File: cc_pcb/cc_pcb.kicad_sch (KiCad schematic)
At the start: 58 parts, among them J1 Conn_02x05_Odd_Even, J2 Controller (40Pin->SPI), J3 Wi-Fi Module, J4 RFID Scanner, J5 SD Card Reader, J6 4x4 Keypad, SW1 SW_Push, U1 LD1117S33TR_SOT223, U2 STM32F091RCTx, U3 LM393

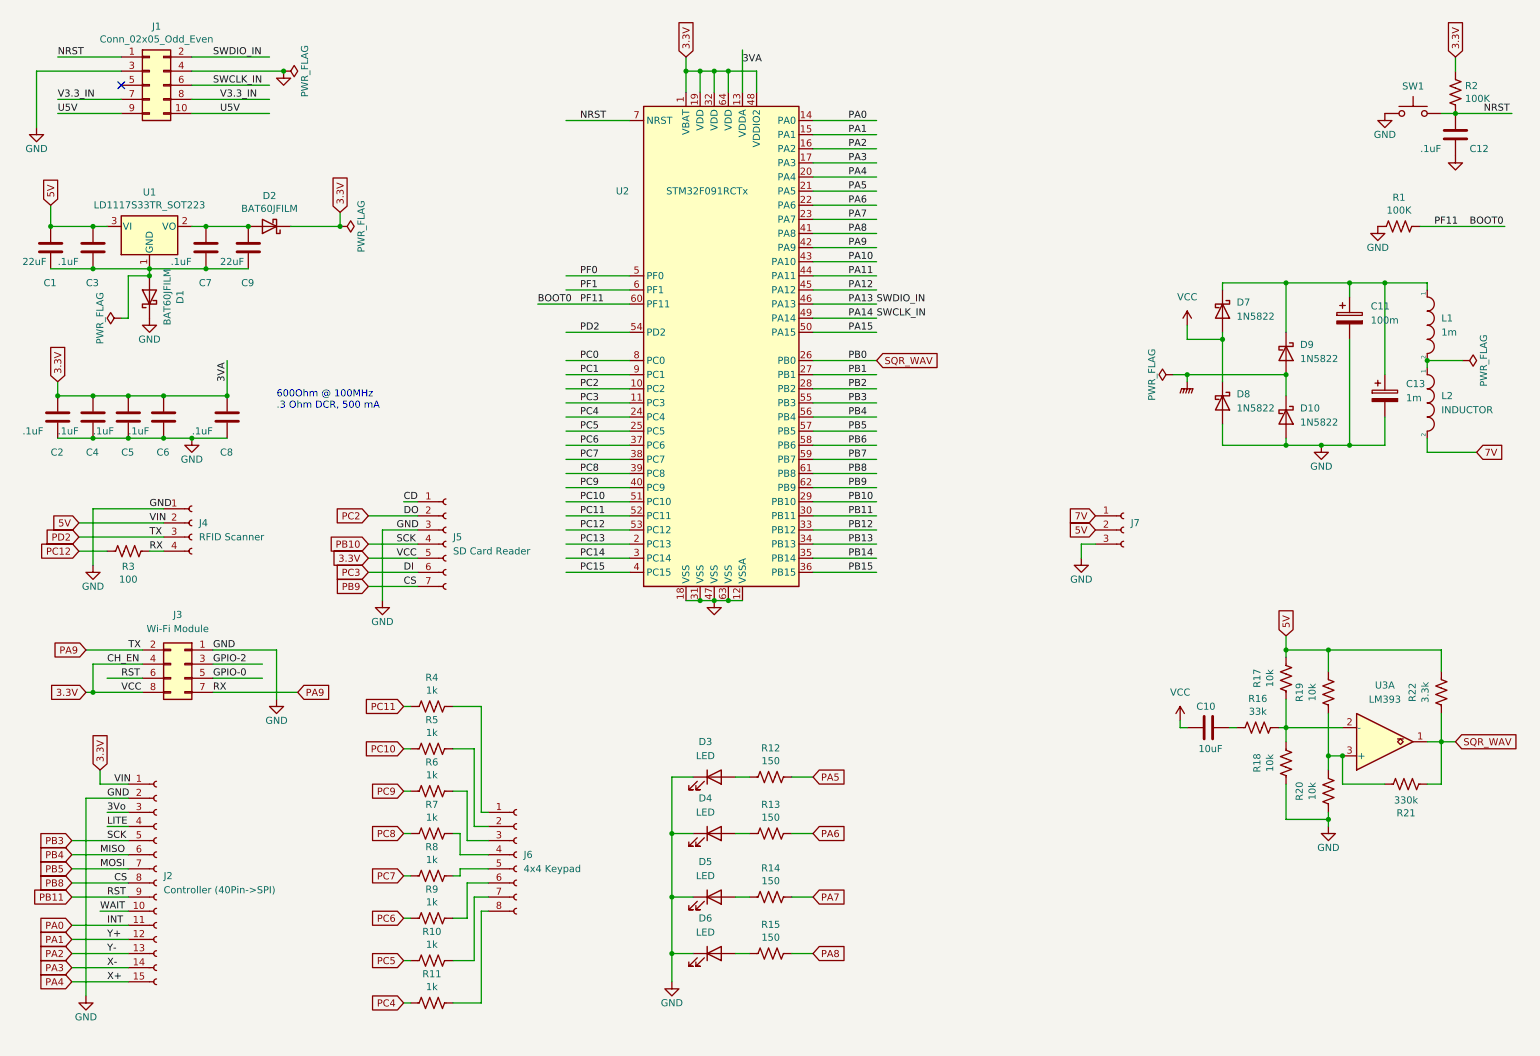
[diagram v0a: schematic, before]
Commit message: organized schematic and separated power supply by modules and our design
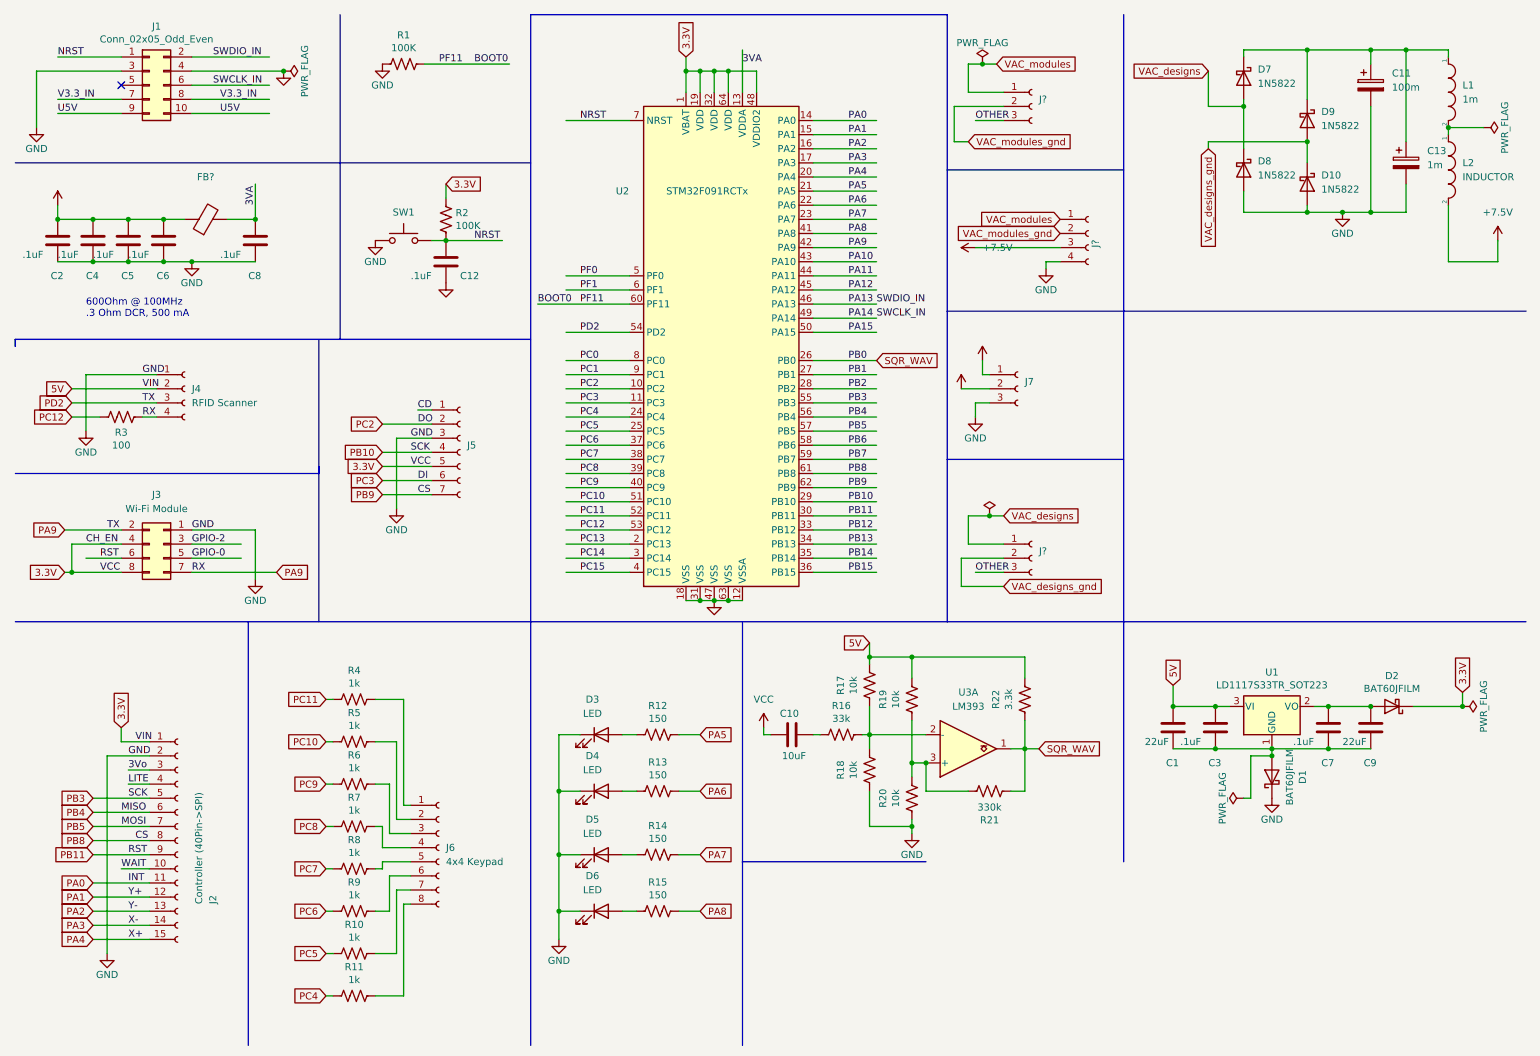
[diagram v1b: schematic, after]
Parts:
- added FB?: (no value), symbol Device:FerriteBead
- added J? (x2): (no value), symbol Connector:Conn_01x03_Female
- added J?: (no value), symbol Connector:Conn_01x04_Female
- J5: value SD Card Reader -> (none)
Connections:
- net GND: now also J?.4 (Pin_4)
- net VCC: no longer C2.1, C4.1, C5.1, C6.1, C8.1, D7.2 (A), D8.1 (K), J7.2 (Pin_2), U2.13 (VDDA)
- net 7V renamed +7.5V
- net +7.5V: now also J?.3 (Pin_3)
- net GNDPWR renamed VAC_designs_gnd
- net VAC_designs_gnd: now also J?.2 (Pin_2)
- new net +3V3: C2.1, C4.1, C5.1, C6.1, FB?.1
- new net +5V: J7.2 (Pin_2)
- new net 3VA: C8.1, FB?.2, U2.13 (VDDA)
- new net OTHER: J?.3 (Pin_3), J?.3 (Pin_3)
- new net VAC_designs: D7.2 (A), D8.1 (K), J?.1 (Pin_1)
- new net VAC_modules: J?.1 (Pin_1), J?.1 (Pin_1)
- new net VAC_modules_gnd: J?.2 (Pin_2), J?.2 (Pin_2)
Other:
- moved on the sheet: C1, C10, C11, C12, C13, C2, C3, C4, C5, C6, C7, C8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

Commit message: buck rectifier circuit (values wrong), changed how power flags were
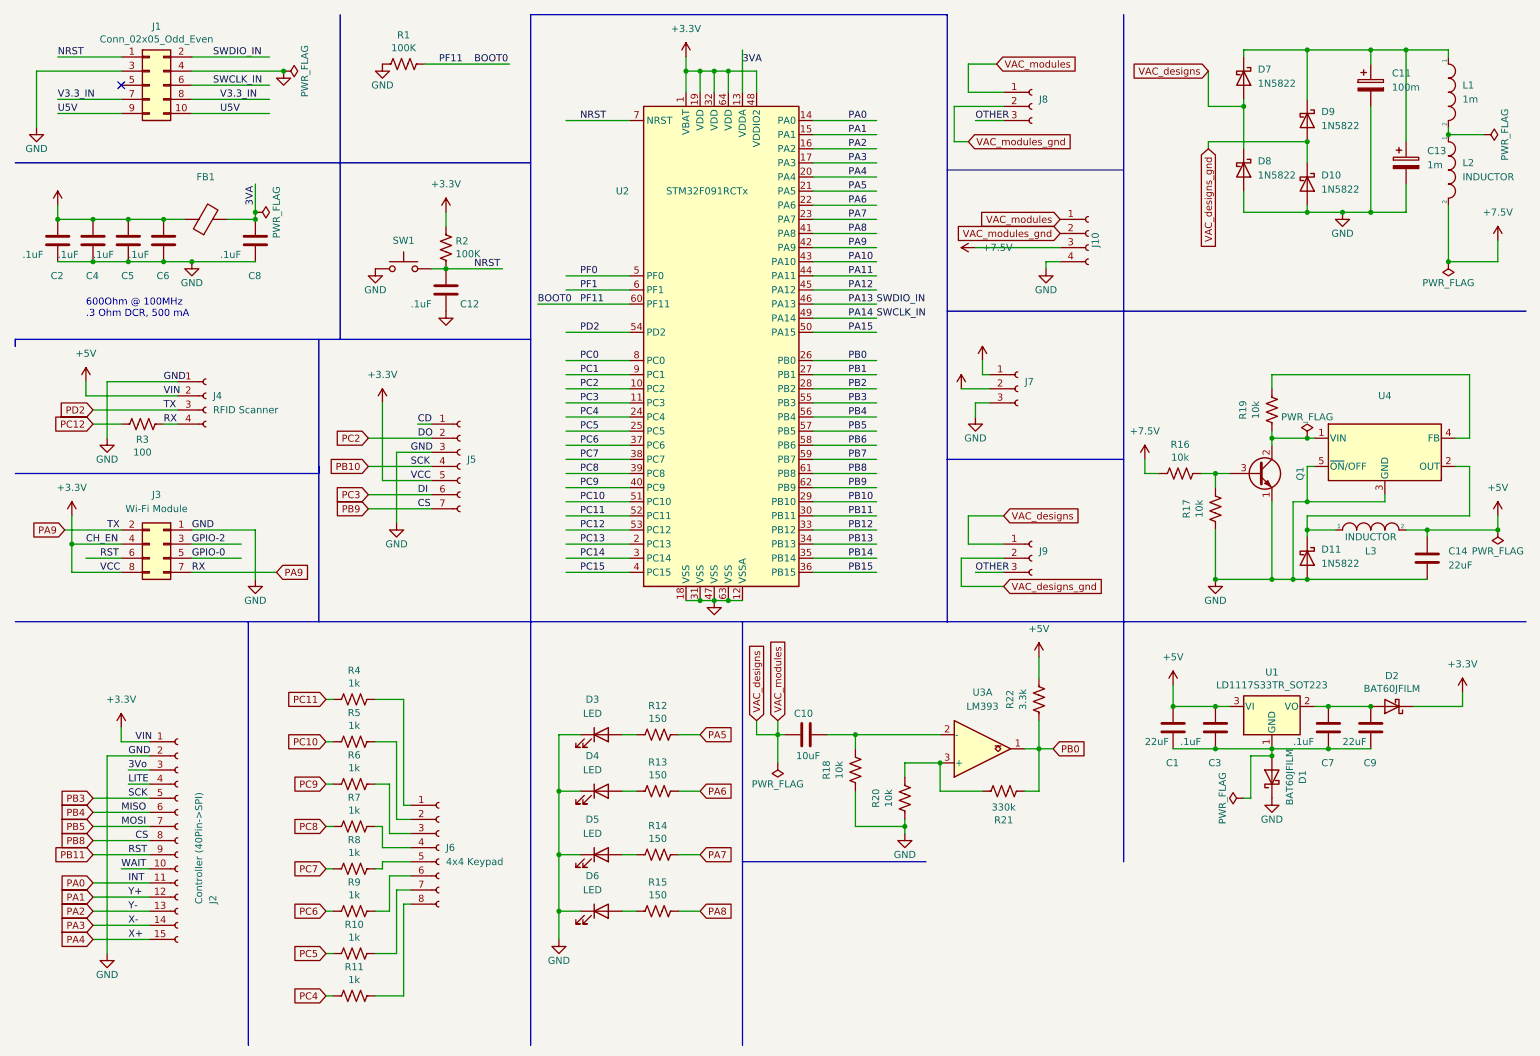
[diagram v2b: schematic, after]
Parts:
- added C14: 22uF, Capacitor_SMD:C_0805_2012Metric_Pad1.18x1.45mm_HandSolder, symbol Device:C
- added D11: 1N5822, imported_footprints:DIO_1N5822, symbol Device:D_Schottky
- added L3: INDUCTOR, symbol pspice:INDUCTOR
- added Q1: (no value), symbol Transistor_BJT:2SC1941
- added U4: (no value), symbol Regulator_Switching:LM2576T-5
- R16: value 33k -> 10k
- gave numbers to parts that had none: 4
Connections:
- net +5V is gone; now on net +3V3: J7.2 (Pin_2)
- net VAC_modules is gone; now on net VAC_designs: J10.1 (Pin_1), J8.1 (Pin_1)
- net +3V3: now also C1.1, C3.1, D2.1 (K), J2.1 (Pin_1), J3.4 (Pin_4), J3.8 (Pin_8), J4.2 (Pin_2), J5.5 (Pin_5), R2.1, R22.1, U1.3 (VI), U2.1 (VBAT), U2.19 (VDD), U2.32 (VDD), U2.48 (VDDIO2), U2.64 (VDD), C14.1, L3.2
- net +7.5V: now also R16.2
- net GND: now also R17.2, C14.2, D11.2 (A), Q1.1 (E), U4.3 (GND), U4.5 (~{ON}/OFF)
- net VAC_designs: now also C10.1
- net at C10.2: now also R18.1, U3.2 (-); no longer R16.2
- net at R20.1, R21.1, U3.3 (+): no longer R19.2
- net SQR_WAV renamed PB0
- removed net VCC: C1.1, C10.1, C3.1, D2.1 (K), J2.1 (Pin_1), J3.4 (Pin_4), J3.8 (Pin_8), J4.2 (Pin_2), J5.5 (Pin_5), R17.1, R19.1, R2.1, R22.1, U1.3 (VI), U2.1 (VBAT), U2.19 (VDD), U2.32 (VDD), U2.48 (VDDIO2), U2.64 (VDD)
- new net: Q1.2 (C), R19.2, U4.1 (VIN)
- new net: Q1.3 (B), R16.1, R17.1
- new net: D11.1 (K), L3.1, U4.2 (OUT)
- new net: R19.1, U4.4 (FB)
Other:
- moved on the sheet: C10, C12, J4, J5, R18, R2, R20, R21, R22, R3, SW1, U3A

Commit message: voltage converter module footrints, all components have footprints, BOM
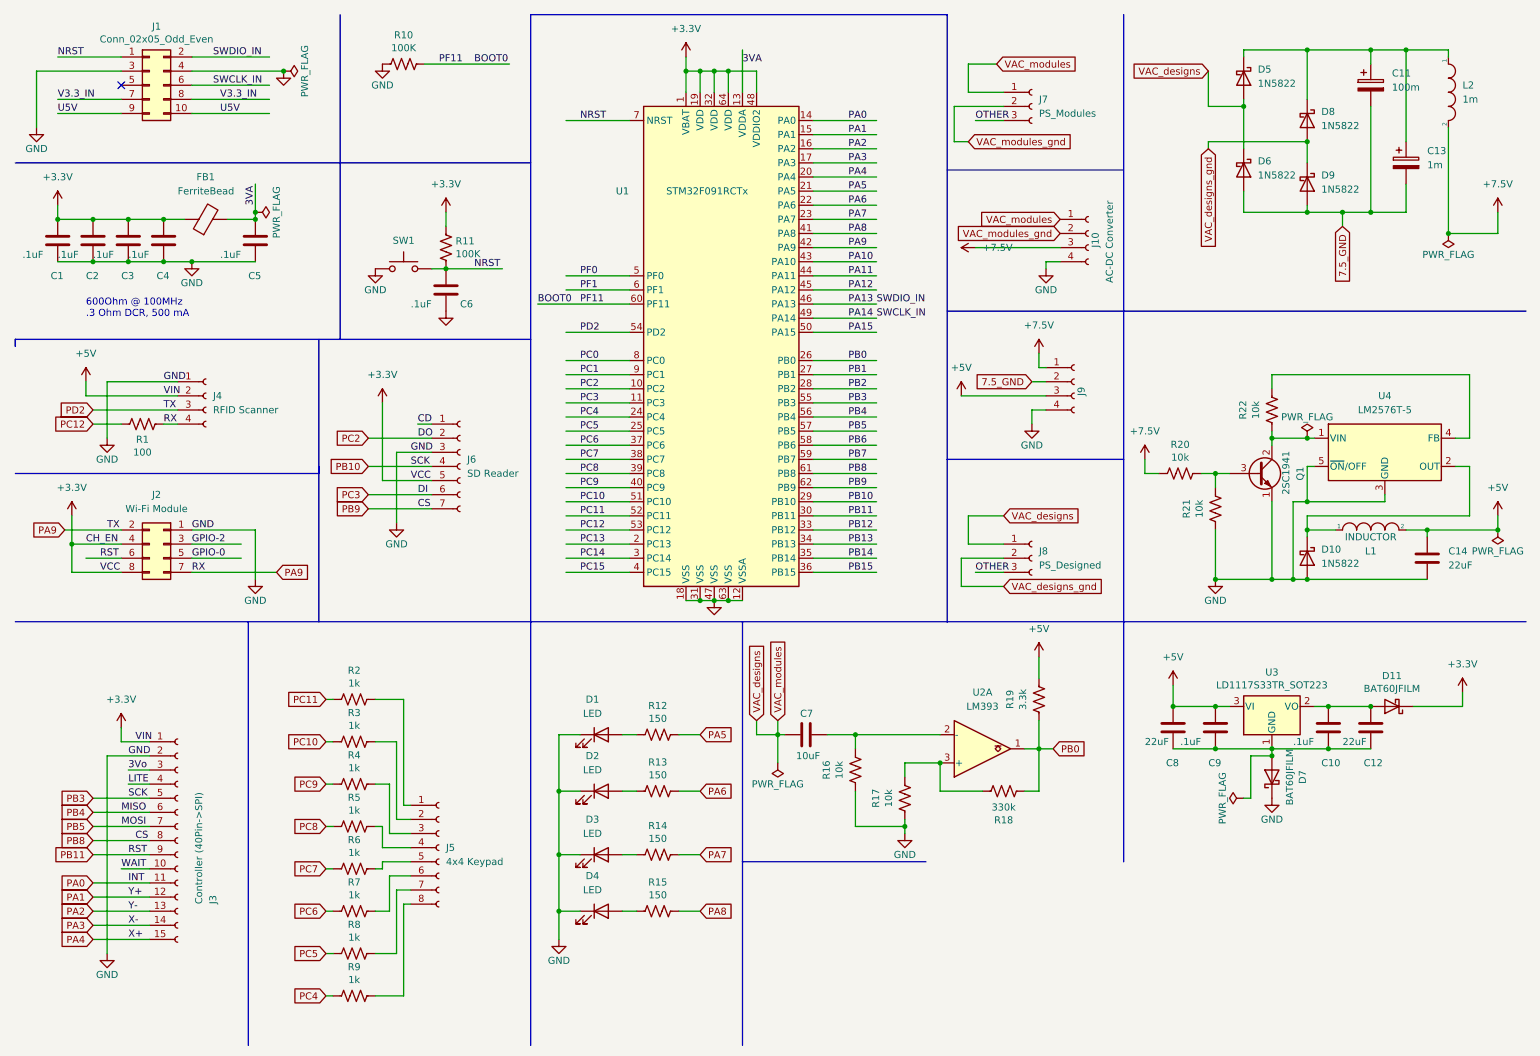
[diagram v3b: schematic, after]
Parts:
- removed J7: (no value), symbol Connector:Conn_01x03_Female
- removed L2: INDUCTOR, symbol pspice:INDUCTOR
- added J9: (no value), symbol Connector:Conn_01x04_Female
- C11: footprint (none) -> Capacitor_THT:CP_Radial_D8.0mm_P3.50mm
- D7: renamed from D1; footprint Diode_SMD:D_SOD-323 -> (none)
- FB1: value (none) -> FerriteBead
- J10: value (none) -> AC-DC Converter
- J3: renamed from J2; footprint imported_footprints:RA8875_TFT_Breakout -> (none)
- J6: renamed from J5; value (none) -> SD Reader; footprint imported_footprints:Micro_SD_card_reader -> (none)
- J7: renamed from J8; value (none) -> PS_Modules
- J8: renamed from J9; value (none) -> PS_Designed
- Q1: value (none) -> 2SC1941; footprint (none) -> Package_TO_SOT_THT:TO-92_Inline
- U1: renamed from U2; footprint Package_QFP:LQFP-64_10x10mm_P0.5mm -> (none)
- U3: renamed from U1; footprint Package_TO_SOT_SMD:SOT-223-3_TabPin2 -> (none)
- U4: value (none) -> LM2576T-5
- renumbered C2 to C1, C7 to C10, C9 to C12, C4 to C2, C5 to C3, C6 to C4, C8 to C5, C12 to C6, C10 to C7, C1 to C8, C3 to C9, D3 to D1, D11 to D10, D2 to D11, D4 to D2, D5 to D3, D6 to D4, D7 to D5, D8 to D6, D9 to D8, D10 to D9, J3 to J2, J6 to J5, L3 to L1, L1 to L2, R3 to R1, R1 to R10, R2 to R11, R18 to R16, R20 to R17, R21 to R18, R22 to R19, R4 to R2, R16 to R20, R17 to R21, R19 to R22, R5 to R3, R6 to R4, R7 to R5, R8 to R6, R9 to R7, R10 to R8, R11 to R9, U3 to U2
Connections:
- net +3V3: now also J9.3 (Pin_3)
- net +7.5V: now also L2.2, J9.1 (Pin_1)
- net GND: now also J9.4 (Pin_4); no longer C11.2, C13.2, D6.2 (A), D9.2 (A)
- new net 7.5_GND: C11.2, C13.2, D6.2 (A), D9.2 (A), J9.2 (Pin_2)

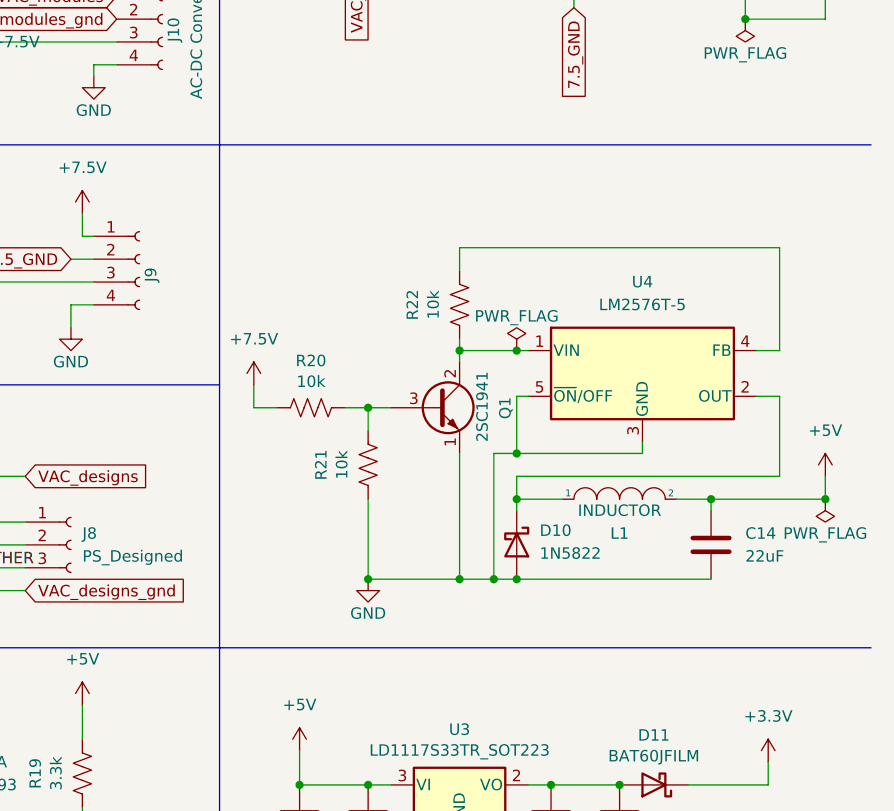
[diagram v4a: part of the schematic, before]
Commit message: TPS56325x schematic symbol and footprint
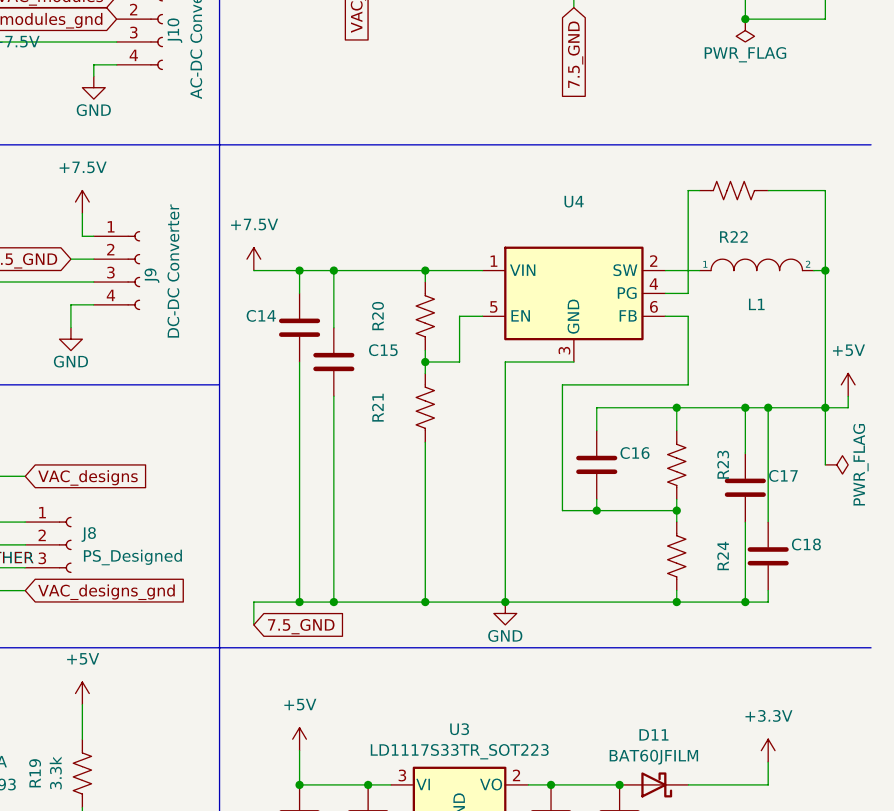
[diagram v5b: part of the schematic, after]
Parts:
- removed D10: 1N5822, imported_footprints:DIO_1N5822, symbol Device:D_Schottky
- removed Q1: 2SC1941, Package_TO_SOT_THT:TO-92_Inline, symbol Transistor_BJT:2SC1941
- removed U4: LM2576T-5, symbol Regulator_Switching:LM2576T-5
- added C15, C16, C17, C18: (no value), Capacitor_SMD:C_0805_2012Metric_Pad1.18x1.45mm_HandSolder, symbol Device:C
- added R23, R24: (no value), Resistor_SMD:R_0805_2012Metric_Pad1.20x1.40mm_HandSolder, symbol Device:R_US
- added U4: (no value), symbol created_schematics:TPS56325x
- C13: footprint (none) -> Capacitor_THT:C_Radial_D18.0mm_H35.5mm_P7.50mm
- C14: value 22uF -> (none)
- D1, D2, D3, D4: footprint (none) -> LED_THT:LED_D3.0mm
- D7: footprint (none) -> Diode_SMD:D_SOD-323
- FB1: footprint (none) -> Ferrite_THT:LairdTech_28C0236-0JW-10
- J10: footprint (none) -> imported_footprints:7.5Vdc-5Vdc_buck_converter
- J2: footprint (none) -> imported_footprints:XCVR_ESP8266-01_ESP-01
- J3: footprint (none) -> imported_footprints:RA8875_TFT_Breakout
- J4: footprint (none) -> imported_footprints:RFID_Reader_PCB
- J5: footprint (none) -> imported_footprints:4x4_keypad
- J6: footprint (none) -> imported_footprints:Micro_SD_card_reader
- J7, J8: footprint (none) -> imported_footprints:barrel_jack_adapter
- J9: value (none) -> DC-DC Converter; footprint (none) -> imported_footprints:7.5Vdc-5Vdc_buck_converter
- L1: value INDUCTOR -> (none); footprint (none) -> Inductor_THT:L_Radial_D7.5mm_P5.00mm_Fastron_07P
- L2: footprint (none) -> Inductor_THT:L_Toroid_Vertical_L54.0mm_W23.8mm_P20.10mm_Bourns_5700
- R20, R21, R22: value 10k -> (none)
- U1: footprint (none) -> Package_QFP:LQFP-64_10x10mm_P0.5mm
- U2: footprint (none) -> imported_footprints:LM393
- U3: footprint (none) -> imported_footprints:5-3.3_buck_converter
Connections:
- net 7.5_GND is gone; now on net GND: C11.2, C13.2, D6.2 (A), D9.2 (A), J9.2 (Pin_2)
- net +3V3: now also R22.2, C16.1, C17.1, C18.1, R23.2; no longer C14.1
- net +7.5V: now also C14.1, R20.1, C15.1, U4.1 (VIN); no longer R20.2
- net GND: now also C15.2, C17.2, C18.2, R24.1, U4.3 (GND)
- net at R21.1: now also R20.2, U4.5 (EN); no longer R20.1
- net at L1.1: now also U4.2 (SW)
- net at R22.1: now also U4.4 (PG)
- new net: C16.2, R23.1, R24.2, U4.6 (FB)
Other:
- moved on the sheet: L1, R20, R21
